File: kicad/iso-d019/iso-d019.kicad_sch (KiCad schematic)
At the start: 36 parts, among them J501 ISO_TO_SYSTEM, K501 G6K-2F DC12, Q501 MMBT3904, Q502 MMBT3904, U501 TPS3700DDC, U502 TPS3700DDC, U503 TMUX6219, U504 TPS3700DDC

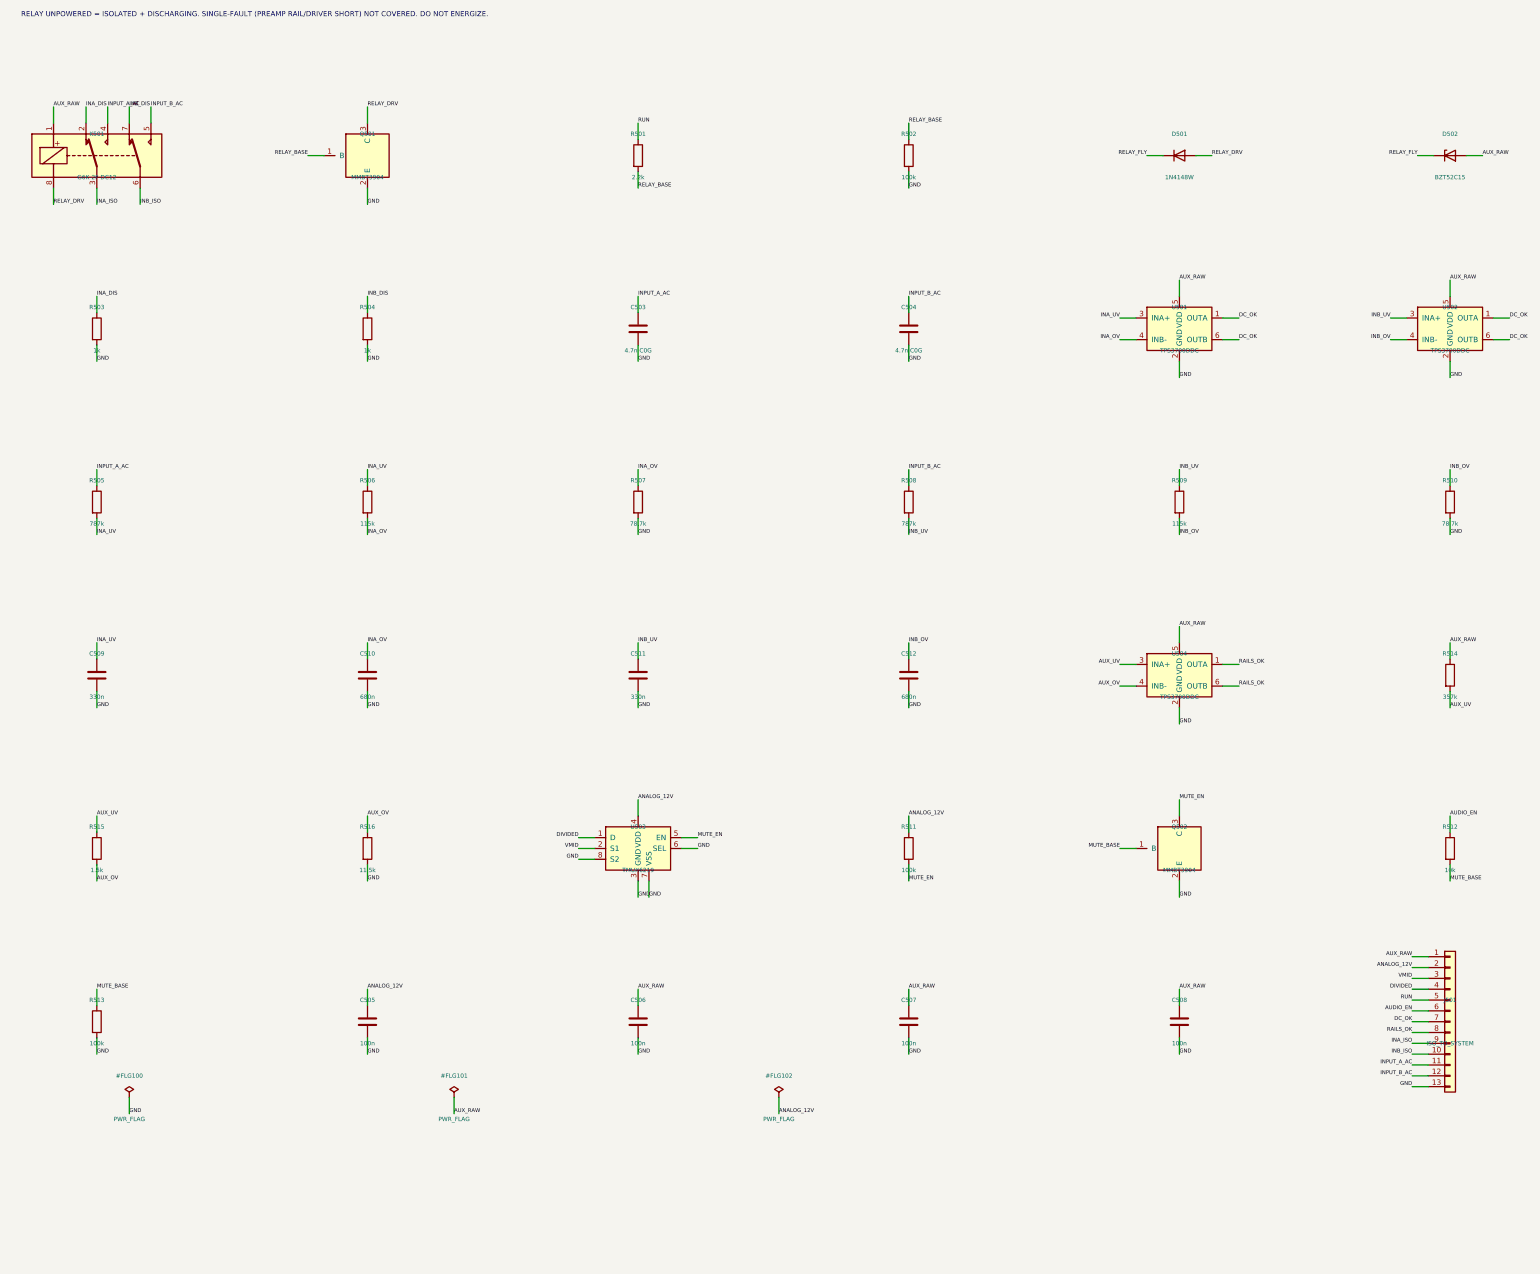
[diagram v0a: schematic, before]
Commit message: feat(eda): clamp TPA inputs against single faults and audit TMUX6219 land pattern
- D-024a: 3.3k series after relay NO plus BAT54 (K on pin, A to GND).
  Driver shorted low with relay closed: about -5.9 V unclamped, <= -0.351 V
  at datasheet maximum VF (still 51 mV beyond -0.3 V); gain -1.33 dB typ.
- simulate_d019: 216 single-fault cases; normal cases now -0.158..6.47 V.
- Local TI DGK0008A footprint (SCDS420E p.50) replaces generic MSOP-8.
- Risk table in iso-d019.md: bounce resolved by design, sub-20 Hz fails
  safe, stuck-high driver and unpowered TPA input remain open.
- system-candidate: 204 footprints, 580 pins matched, DRC 0; gallery and
  SVG regenerated.
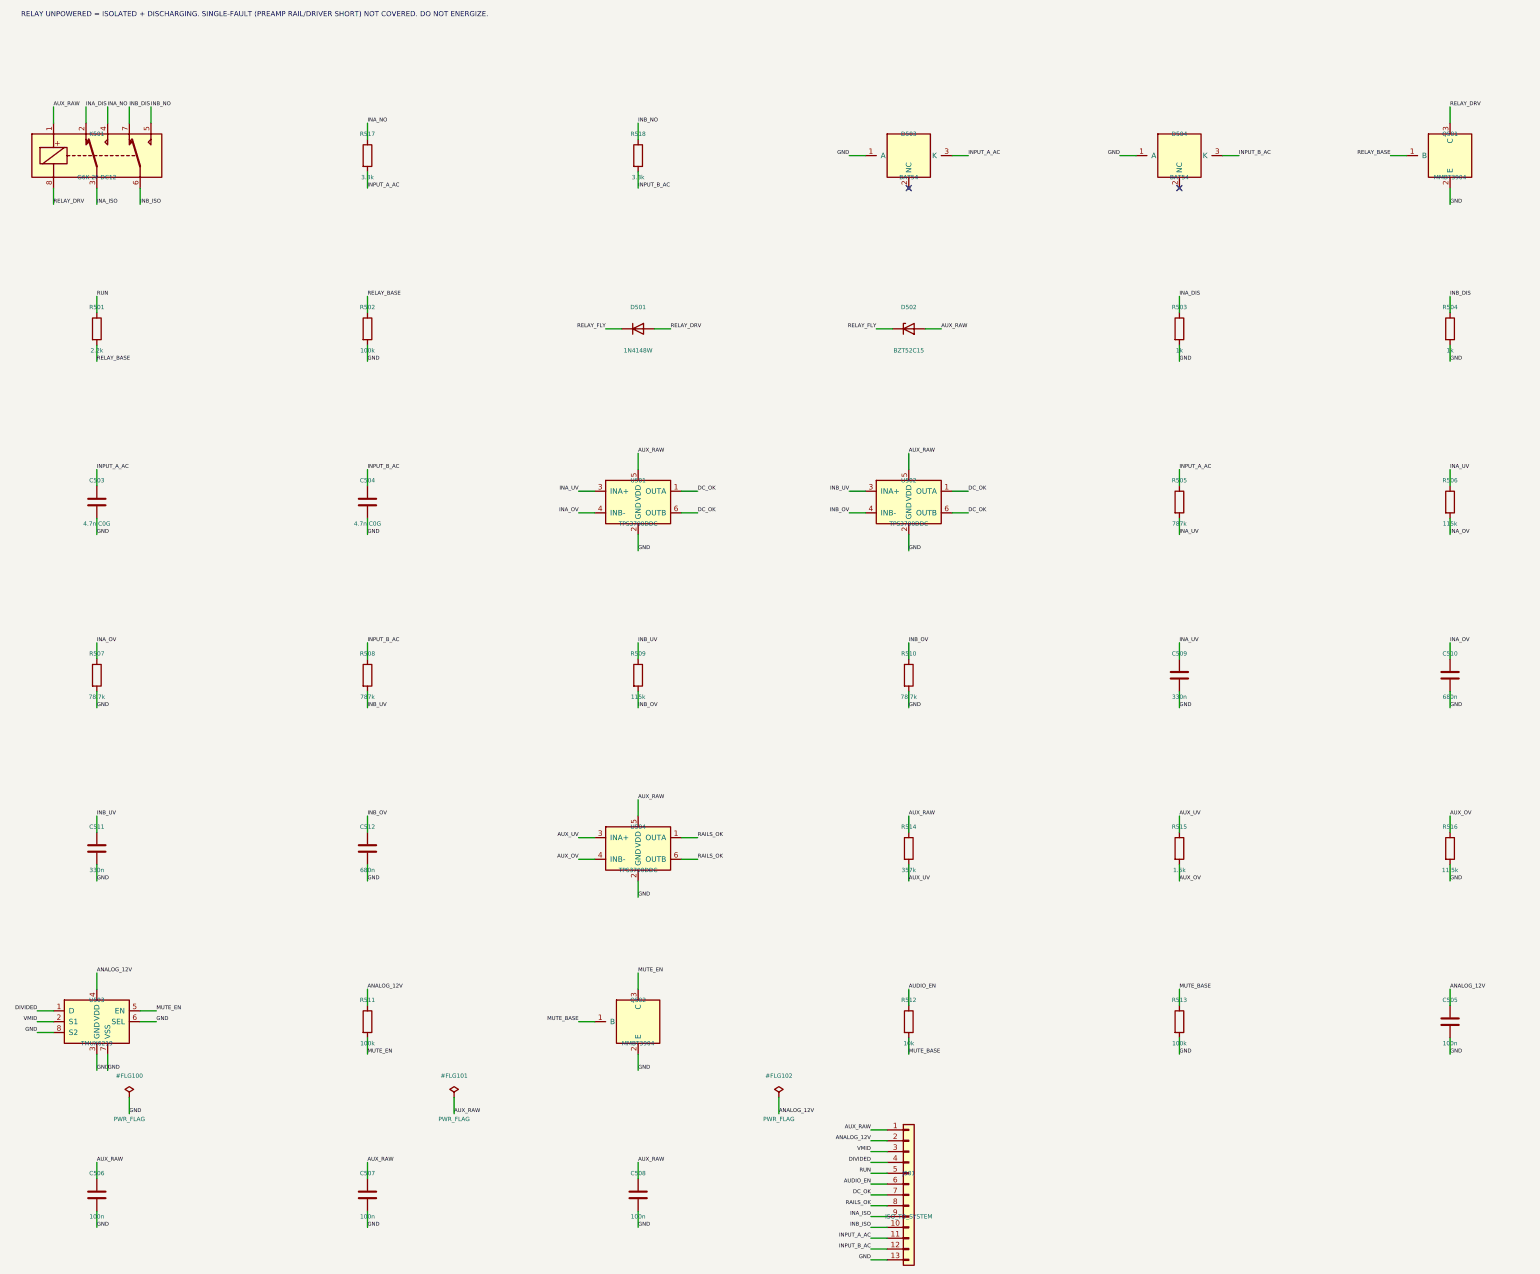
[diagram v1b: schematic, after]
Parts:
- added D503, D504: BAT54, Package_TO_SOT_SMD:SOT-23, symbol PS28_ISO:BAT54
- added R517, R518: 3.3k, Resistor_SMD:R_0603_1608Metric, symbol Device:R
- U503: footprint Package_SO:MSOP-8_3x3mm_P0.65mm -> PS28_ANALOG:TI_DGK0008A
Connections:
- net GND: now also D503.1 (A), D504.1 (A)
- net INPUT_A_AC: now also D503.3 (K), R517.2; no longer K501.4
- net INPUT_B_AC: now also D504.3 (K), R518.2; no longer K501.5
- new net INA_NO: K501.4, R517.1
- new net INB_NO: K501.5, R518.1
- no-connect marks 0 -> 2
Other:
- moved on the sheet: C503, C504, C505, C506, C507, C508, C509, C510, C511, C512, D501, D502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
